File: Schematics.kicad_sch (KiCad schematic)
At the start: 44 parts, among them Q1 AO3400A, Q2 AO3401A

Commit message: added a missing capacitor
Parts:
- added C29: CL31A107MQHNNNE, local:C1206, symbol local:CL31A107MQHNNNE
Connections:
- net GND: now also C29.1
- net V_B: now also C29.2
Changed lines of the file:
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@@
 	)
 	(junction
+		(at 209.55 33.02)
+		(diameter 0)
+		(color 0 0 0 0)
+	)
+	(junction
 		(at 73.66 81.28)
 		(diameter 0)
@@
 	(wire
 		(pts
+			(xy 209.55 33.02) (xy 209.55 36.83)
+		)
+		(stroke
+			(width 0)
+			(type default)
+		)
+	)
+	(wire
+		(pts
 			(xy 44.45 81.28) (xy 60.96 81.28)
 		)
@@
 	)
 	(symbol
+		(lib_id "power:GND")
+		(at 209.55 44.45 0)
+		(unit 1)
+		(body_style 1)
+		(exclude_from_sim no)
+		(in_bom yes)
+		(on_board yes)
+		(in_pos_files yes)
+		(dnp no)
+		(fields_autoplaced yes)
+		(property "Reference" "#PWR09"
+			(at 209.55 50.8 0)
+			(hide yes)
+			(show_name no)
+			(do_not_autoplace no)
+			(effects
+				(font
+					(size 1.27 1.27)
+				)
+			)
+		)
+		(property "Value" "GND"
+			(at 209.55 49.53 0)
+			(show_name no)
+			(do_not_autoplace no)
+			(effects
+				(font
+					(size 1.27 1.27)
+				)
+			)
+		)
+		(property "Footprint" ""
+			(at 209.55 44.45 0)
+			(hide yes)
+			(show_name no)
+			(do_not_autoplace no)
+			(effects
+				(font
+					(size 1.27 1.27)
+				)
+			)
+		)
+		(property "Datasheet" ""
+			(at 209.55 44.45 0)
+			(hide yes)
+			(show_name no)
+			(do_not_autoplace no)
+			(effects
+				(font
+					(size 1.27 1.27)
+				)
+			)
+		)
+		(property "Description" "Power symbol creates a global label with name \"GND\" , ground"
+			(at 209.55 44.45 0)
+			(hide yes)
+			(show_name no)
+			(do_not_autoplace no)
+			(effects
+				(font
+					(size 1.27 1.27)
+				)
+			)
+		)
+		(pin "1"
+		)
+		(instances
+			(project "Schematics"
+				(path "/ba81e668-39a3-44b1-9436-fbe95b38ede8"
+					(reference "#PWR09")
+					(unit 1)
+				)
+			)
+		)
+	)
+	(symbol
 		(lib_id "Device:C_Small")
 		(at 62.23 119.38 90)
@@
 					(unit 1)
 				)
+			)
+		)
+	)
+	(symbol
+		(lib_id "local:CL31A107MQHNNNE")
+		(at 209.55 40.64 90)
+		(unit 1)
+		(body_style 1)
+		(exclude_from_sim no)
+		(in_bom yes)
+		(on_board yes)
+		(in_pos_files yes)
+		(dnp no)
+		(fields_autoplaced yes)
+		(property "Reference" "C29"
+			(at 213.36 39.3699 90)
+			(show_name no)
+			(do_not_autoplace no)
+			(effects
+				(font
+					(size 1.27 1.27)
+				)
+				(justify right)
+			)
+		)
+		(property "Value" "CL31A107MQHNNNE"
+			(at 213.36 41.9099 90)
+			(show_name no)
+			(do_not_autoplace no)
+			(effects
+				(font
+					(size 1.27 1.27)
+				)
+				(justify right)
+			)
+		)
+		(property "Footprint" "local:C1206"
+			(at 217.17 40.64 0)
+			(hide yes)
+			(show_name no)
+			(do_not_autoplace no)
+			(effects
+				(font
+					(size 1.27 1.27)
+				)
+			)
+		)
+		(property "Datasheet" "https://lcsc.com/product-detail/Multilayer-Ceramic-Capacitors-MLCC-SMD-SMT_SAMSUNG_CL31A107MQHNNNE_100uF-107-20-6-3V_C15008.html"
+			(at 219.71 40.64 0)
+			(hide yes)
+			(show_name no)
+			(do_not_autoplace no)
+			(effects
+				(font
+					(size 1.27 1.27)
+				)
+			)
+		)
+		(property "Description" "100uF (107) ±20% 6.3V"
+			(at 209.55 40.64 0)
+			(hide yes)
+			(show_name no)
+			(do_not_autoplace no)
+			(effects
+				(font
+					(size 1.27 1.27)
+				)
+			)
+		)
+		(property "Manufacturer" "SAMSUNG(三星)"
+			(at 222.25 40.64 0)
+			(hide yes)
+			(show_name no)
+			(do_not_autoplace no)
+			(effects
+				(font
+					(size 1.27 1.27)
+				)
+			)
+		)
+		(property "MPN" "CL31A107MQHNNNE"
+			(at 224.79 40.64 0)
+			(hide yes)
+			(show_name no)
+			(do_not_autoplace no)
+			(effects
+				(font
+					(size 1.27 1.27)
+				)
+			)
+		)
+		(property "LCSC Part" "C15008"
+			(at 227.33 40.64 0)
+			(hide yes)
+			(show_name no)
+			(do_not_autoplace no)
+			(effects
+				(font
+					(size 1.27 1.27)
+				)
+			)
+		)
+		(pin "1"
+		)
+		(pin "2"
+		)
+		(instances
+			(project "Schematics"
+				(path "/ba81e668-39a3-44b1-9436-fbe95b38ede8"
+					(reference "C29")
+					(unit 1)
+				)

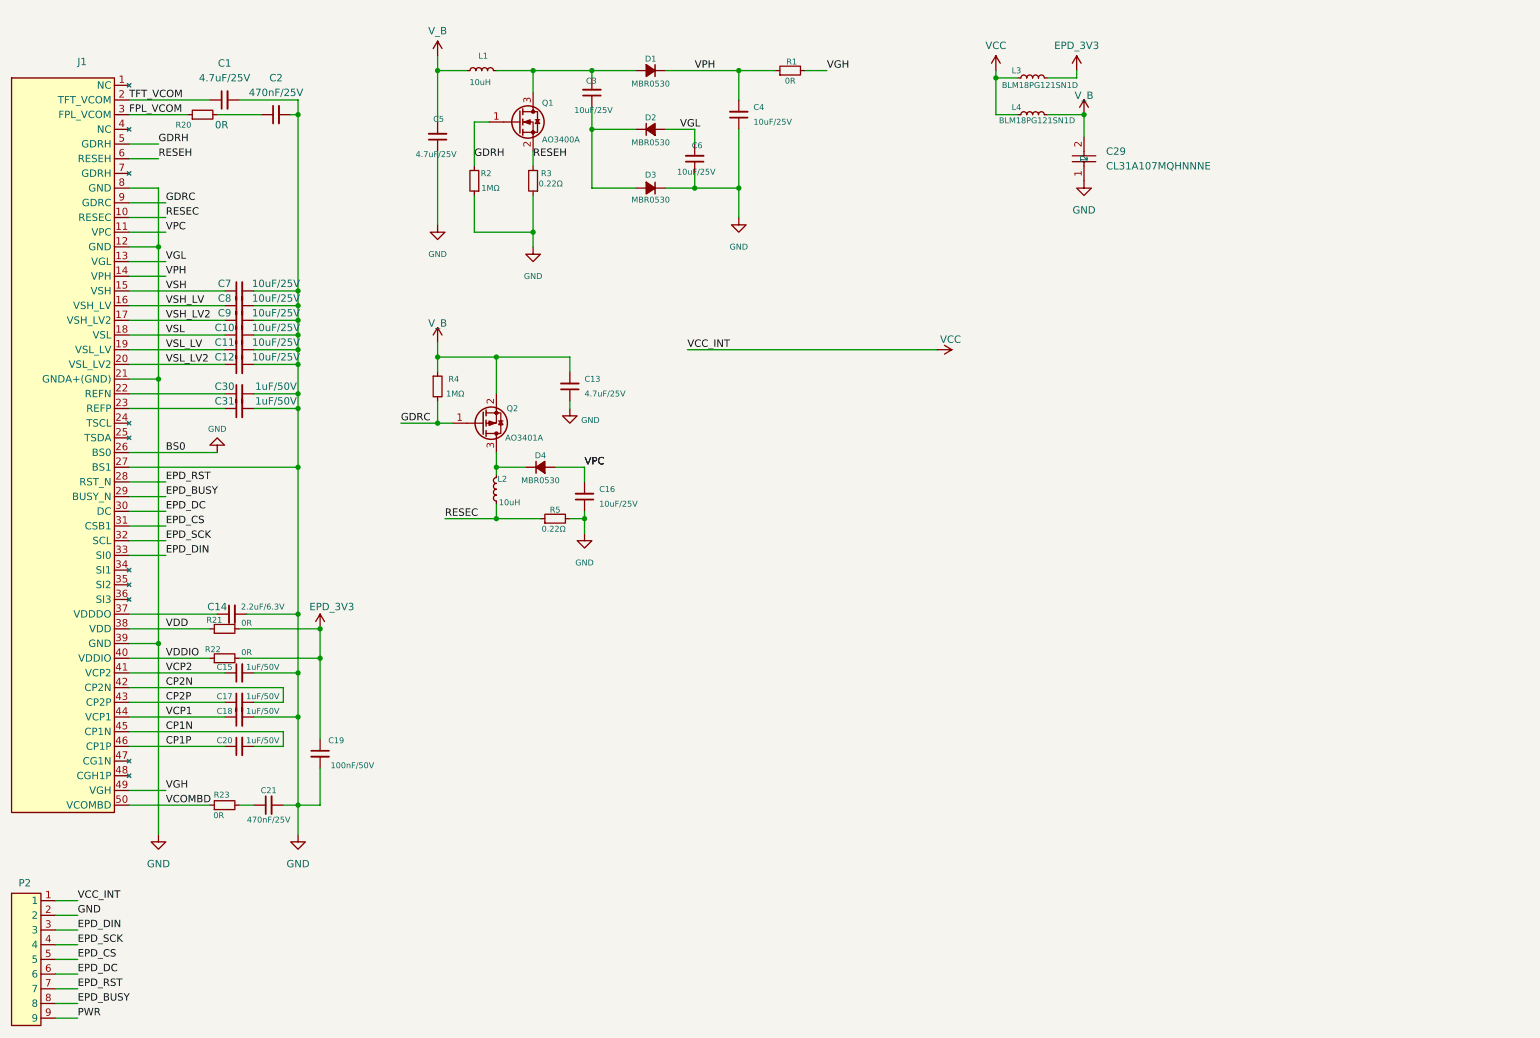
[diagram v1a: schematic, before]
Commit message: added missing capacitor
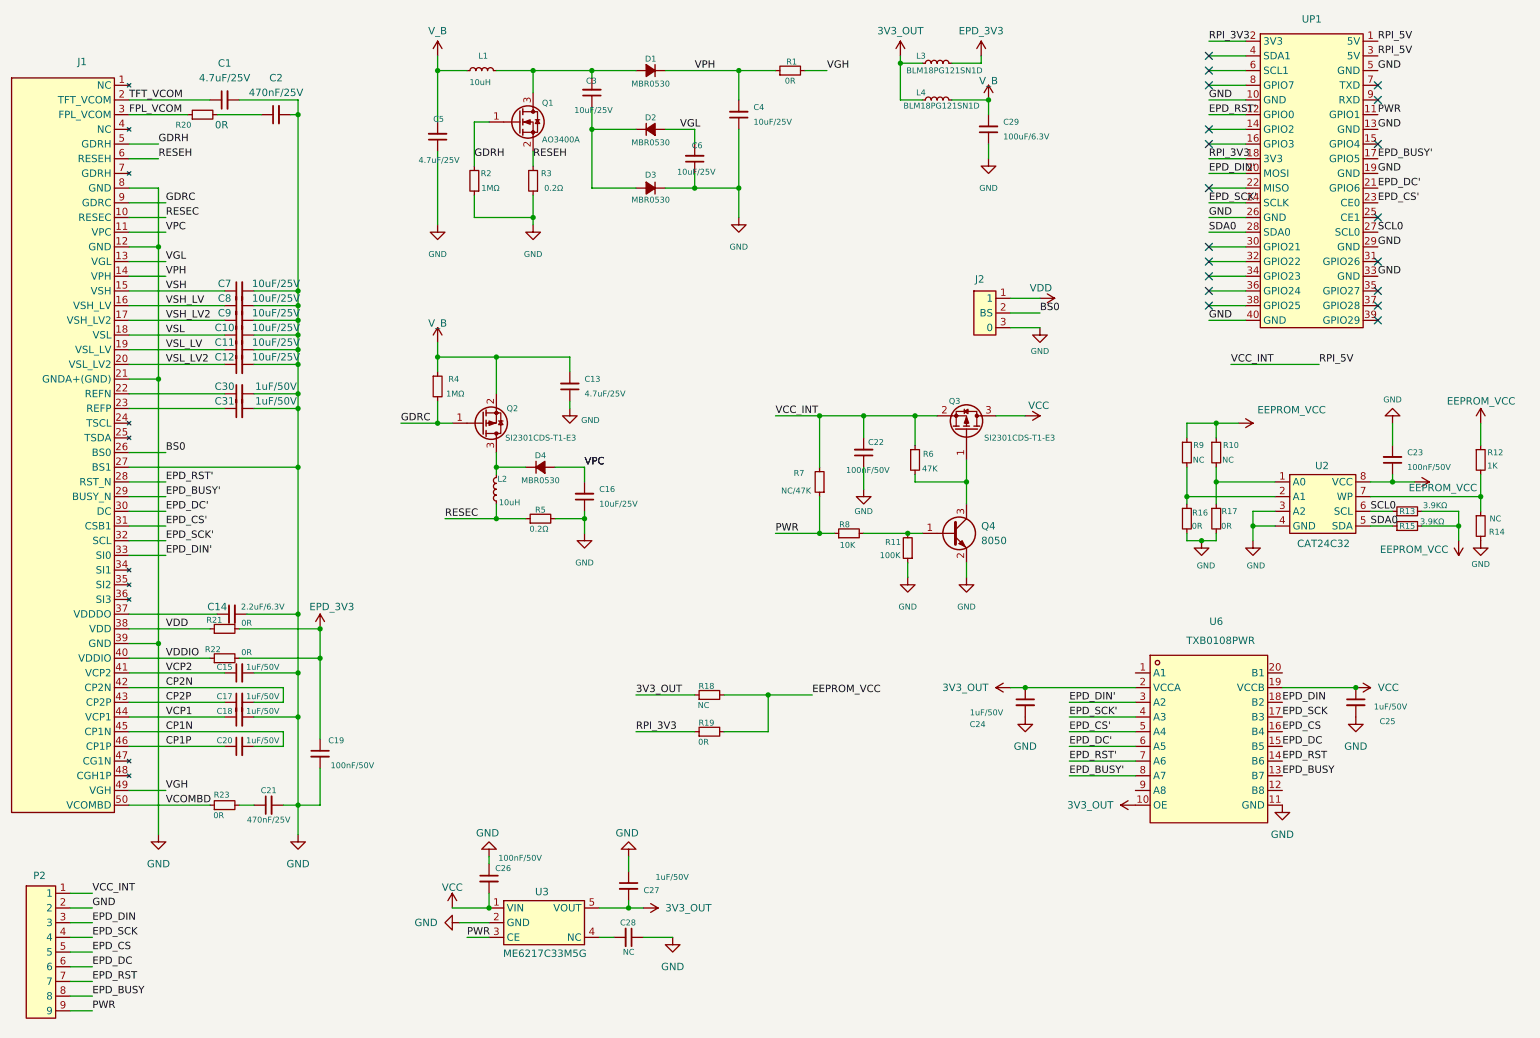
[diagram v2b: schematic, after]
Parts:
- removed C29: CL31A107MQHNNNE, local:C1206, symbol local:CL31A107MQHNNNE
- added C22, C23, C26: 100nF/50V, Capacitor_SMD:C_0603_1608Metric, symbol Device:C_Small
- added C24, C25, C27: 1uF/50V, Capacitor_SMD:C_0603_1608Metric, symbol Device:C_Small
- added C28: NC, Capacitor_SMD:C_0603_1608Metric, symbol Device:C_Small
- added C29: 100uF/6.3V, Capacitor_SMD:C_1206_3216Metric, symbol Device:C_Small
- added J2: (no value), Connector_PinSocket_2.54mm:PinSocket_1x03_P2.54mm_Vertical, symbol Hat_Eink_Esp32:Eink_Esp32_Switch
- added Q3: SI2301CDS-T1-E3, local:SOT-23_L2.9-W1.3-P1.90-LS2.4-BR, symbol Transistor_FET:Q_PMOS_GSD
- added Q4: 8050, local:SOT-23-3_L3.0-W1.7-P0.95-LS2.9-BR, symbol Transistor_BJT:SS8050
- added R10, R14, R18, R9: NC, Resistor_SMD:R_0603_1608Metric, symbol Device:R_Small
- added R11: 100K, Resistor_SMD:R_0603_1608Metric, symbol Device:R_Small
- added R12: 1K, Resistor_SMD:R_0603_1608Metric, symbol Device:R_Small
- added R13, R15: 3.9KΩ, Resistor_SMD:R_0603_1608Metric, symbol Device:R_Small
- added R16, R17, R19: 0R, Resistor_SMD:R_0603_1608Metric, symbol Device:R_Small
- added R6: 47K, Resistor_SMD:R_0603_1608Metric, symbol Device:R_Small
- added R7: NC/47K, Resistor_SMD:R_0603_1608Metric, symbol Device:R_Small
- added R8: 10K, Resistor_SMD:R_0603_1608Metric, symbol Device:R_Small
- added U2: CAT24C32, local:SOIC-8_L5.0-W4.0-P1.27-LS6.0-BL, symbol Hat_Eink_Esp32:Eink_Esp32_CAT24C32
- added U3: ME6217C33M5G, local:SOT-23-5_L3.0-W1.7-P0.95-LS2.8-BR, symbol Hat_Eink_Esp32:Eink_Esp32_ME6217C33M5G
- added U6: TXB0108PWR, local:TSSOP-20_L6.5-W4.4-P0.65-LS6.4-BL, symbol local:TXB0108PWR
- added UP1: (no value), local:HDR-SMD_40P-P2.54-V-F-R2-C20-S2.54-LS7.1, symbol Hat_Eink_Esp32:Eink_Esp32_Rpi
- C1, C13, C5: footprint Capacitor_SMD:C_0805_2012Metric -> Capacitor_SMD:C_0603_1608Metric
- C14: footprint Capacitor_SMD:C_0402_1005Metric -> Capacitor_SMD:C_0603_1608Metric
- D1, D2, D3, D4: footprint local:SOD-123_L2.7-W1.6-LS3.7-RD-1 -> local:SOD-123_L2.8-W1.8-LS3.7-RD
- L1, L2: footprint local:L0805 -> Inductor_SMD:L_1008_2520Metric
- Q2: value AO3401A -> SI2301CDS-T1-E3; footprint local:SOT-23-3_L2.9-W1.3-P1.90-LS2.4-BR -> local:SOT-23_L2.9-W1.3-P1.90-LS2.4-BR
- R3, R5: value 0.22Ω -> 0.2Ω; footprint Resistor_SMD:R_0805_2012Metric -> Resistor_SMD:R_0603_1608Metric
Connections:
- net EPD_BUSY: now also U6.13 (B7); no longer J1.29 (BUSY_N)
- net EPD_CS: now also U6.16 (B4); no longer J1.31 (CSB1)
- net EPD_DC: now also U6.15 (B5); no longer J1.30 (DC)
- net EPD_DIN: now also U6.18 (B2); no longer J1.33 (SI0)
- net EPD_RST: now also U6.14 (B6); no longer J1.28 (RST_N)
- net EPD_SCK: now also U6.17 (B3); no longer J1.32 (SCL)
- net GND: now also C22.1, C23.2, C24.2, C25.2, C26.1, C27.1, C28.1, C29.1, J2.3 (0), Q4.2 (E), R11.1, R14.2, R16.2, R17.2, U2.3 (A2), U2.4 (GND), U3.2 (GND), U6.11 (GND), UP1.10 (GND), UP1.13 (GND), UP1.19 (GND), UP1.26 (GND), UP1.29 (GND), UP1.33 (GND), UP1.40 (GND), UP1.5 (GND); no longer J1.26 (BS0)
- net PWR: now also R7.1, R8.1, U3.3 (CE), UP1.11 (GPIO1)
- net VCC: now also C25.1, C26.2, Q3.3 (D), U3.1 (VIN), U6.19 (VCCB); no longer L3.1, L4.1, P2.1
- net VDD: now also J2.1
- net V_B: now also C29.2
- new net: R12.2, R14.1, U2.7 (WP)
- new net: R16.1, R9.2, U2.2 (A1)
- new net: C28.2, U3.4 (NC)
- new net: Q3.1 (G), Q4.3 (C), R6.2
- new net: R10.2, R17.1, U2.1 (A0)
- new net: Q4.1 (B), R11.2, R8.2
- new net 3V3_OUT: C24.1, C27.2, L3.1, L4.1, R18.1, U3.5 (VOUT), U6.10 (OE), U6.2 (VCCA)
- new net BS0: J1.26 (BS0), J2.2 (BS)
- new net EEPROM_VCC: C23.1, R10.1, R12.1, R13.2, R15.2, R18.2, R19.2, R9.1, U2.8 (VCC)
- new net EPD_BUSY': J1.29 (BUSY_N), U6.8 (A7), UP1.17 (GPIO5)
- new net EPD_CS': J1.31 (CSB1), U6.5 (A4), UP1.23 (CE0)
- new net EPD_DC': J1.30 (DC), U6.6 (A5), UP1.21 (GPIO6)
- new net EPD_DIN': J1.33 (SI0), U6.3 (A2), UP1.20 (MOSI)
- new net EPD_RST': J1.28 (RST_N), U6.7 (A6), UP1.12 (GPIO0)
- new net EPD_SCK': J1.32 (SCL), U6.4 (A3), UP1.24 (SCLK)
- new net RPI_3V3: R19.1, UP1.18 (3V3), UP1.2 (3V3)
- new net RPI_5V: C22.2, P2.1, Q3.2 (S), R6.1, R7.2, UP1.1 (5V), UP1.3 (5V)
- new net SCL0: R13.1, U2.6 (SCL), UP1.27 (SCL0)
- new net SDA0: R15.1, U2.5 (SDA), UP1.28 (SDA0)
- no-connect marks 0 -> 19
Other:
- moved on the sheet: L3, L4, P2, R5
